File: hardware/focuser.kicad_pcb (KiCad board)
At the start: 2 copper layers, 61 x 41.3 mm, 24 parts, among them IC1 AT90USB162-A, J1 USB, P1 Power, P2 Motor, P3 ISP, Q1 IRML9301TFPbF, U1 A4988, U2 MC78L05A, U3 RECEIVER, X1 8MHz

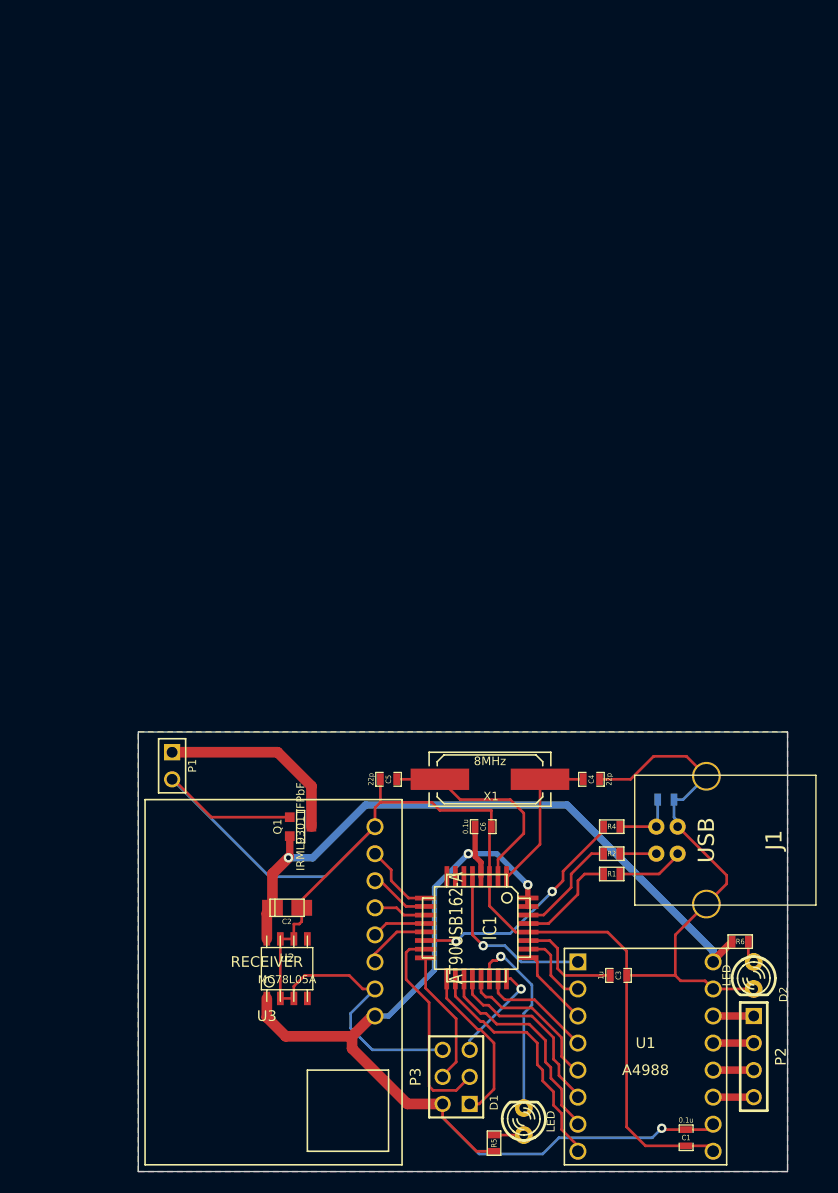
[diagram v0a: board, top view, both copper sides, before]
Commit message: make manufacturable boards (according to Eurocircuit's rules)
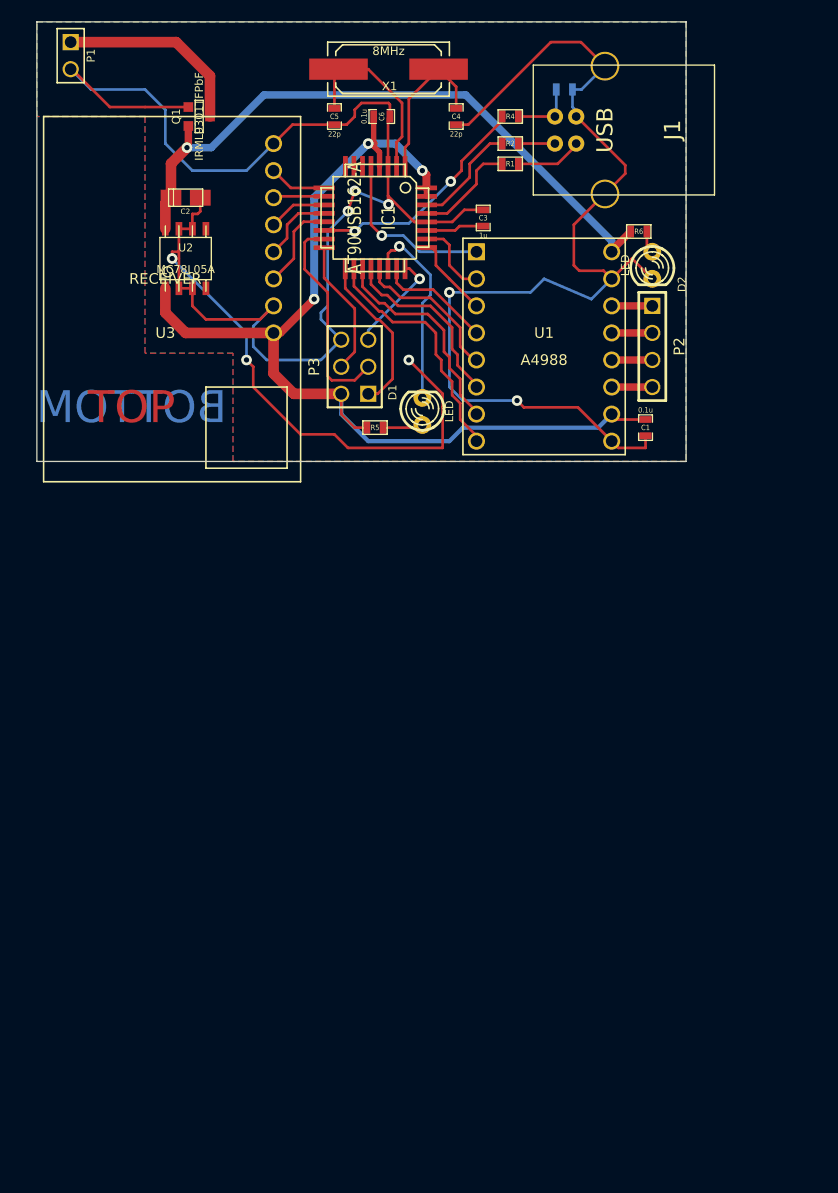
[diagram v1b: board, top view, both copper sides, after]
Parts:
- moved C3 72.2 mm to (149.9, 102.9), turned to 90 degrees
- moved R5 68.1 mm to (139.7, 122.6), turned to 180 degrees
- moved C6 67.4 mm to (140.3, 93.3)
- moved P1 67.4 mm to (111.1, 87.6)
- moved Q1 67.4 mm to (123.2, 93.3)
- moved R4 67.4 mm to (152.4, 93.3)
- moved U1 67.4 mm to (155.6, 114.9)
- moved D2 67.4 mm to (165.7, 107.3)
- moved J1 67.4 mm to (161.3, 94.6)
- moved P2 67.4 mm to (165.7, 114.9)
- moved R1 67.4 mm to (152.4, 97.8)
- moved R2 67.4 mm to (152.4, 95.9)
- moved R6 67.4 mm to (164.5, 104.1)
- moved C2 67.4 mm to (121.9, 101.0)
- moved IC1 67.4 mm to (139.7, 102.9)
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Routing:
- net GND: track 196.6 -> 272.9 mm, vias 0 -> 8
- net N-0000029: track 10.2 -> 5.50 mm
- net N-000002: track 20.2 -> 17.3 mm
- net N-0000020: track 6.36 -> 8.46 mm
- net N-0000021: track 5.19 -> 6.99 mm
- net +5V: track 96.1 -> 97.8 mm
- net N-0000024: track 7.07 -> 5.42 mm
- net N-0000013: track 2.79 -> 3.79 mm
- net N-0000023: track 5.75 -> 4.80 mm
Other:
- net class Default: via_dia 0.889 -> 1
- net class Power: trace_width 1 -> 0.4; via_dia 0.889 -> 1
- rule via_min_drill: 0.508 -> 0.63
- rule via_min_size: 0.889 -> 1
- board text added: "BOTTOM"
- board text added: "TOP"
